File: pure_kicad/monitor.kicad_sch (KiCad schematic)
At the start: 48 parts, among them J3 XT60M, J4 XT60M, J5 Conn_01x04_Pin, J6 Conn_01x04_Pin, J7 Pack Thermistor 1, J8 Pack Thermistor 2, Q5 Q_PMOS_SGD, Q6 Q_NMOS_DGS, Q7 Q_NMOS_DGS, U2 BQ40Z80RSMR

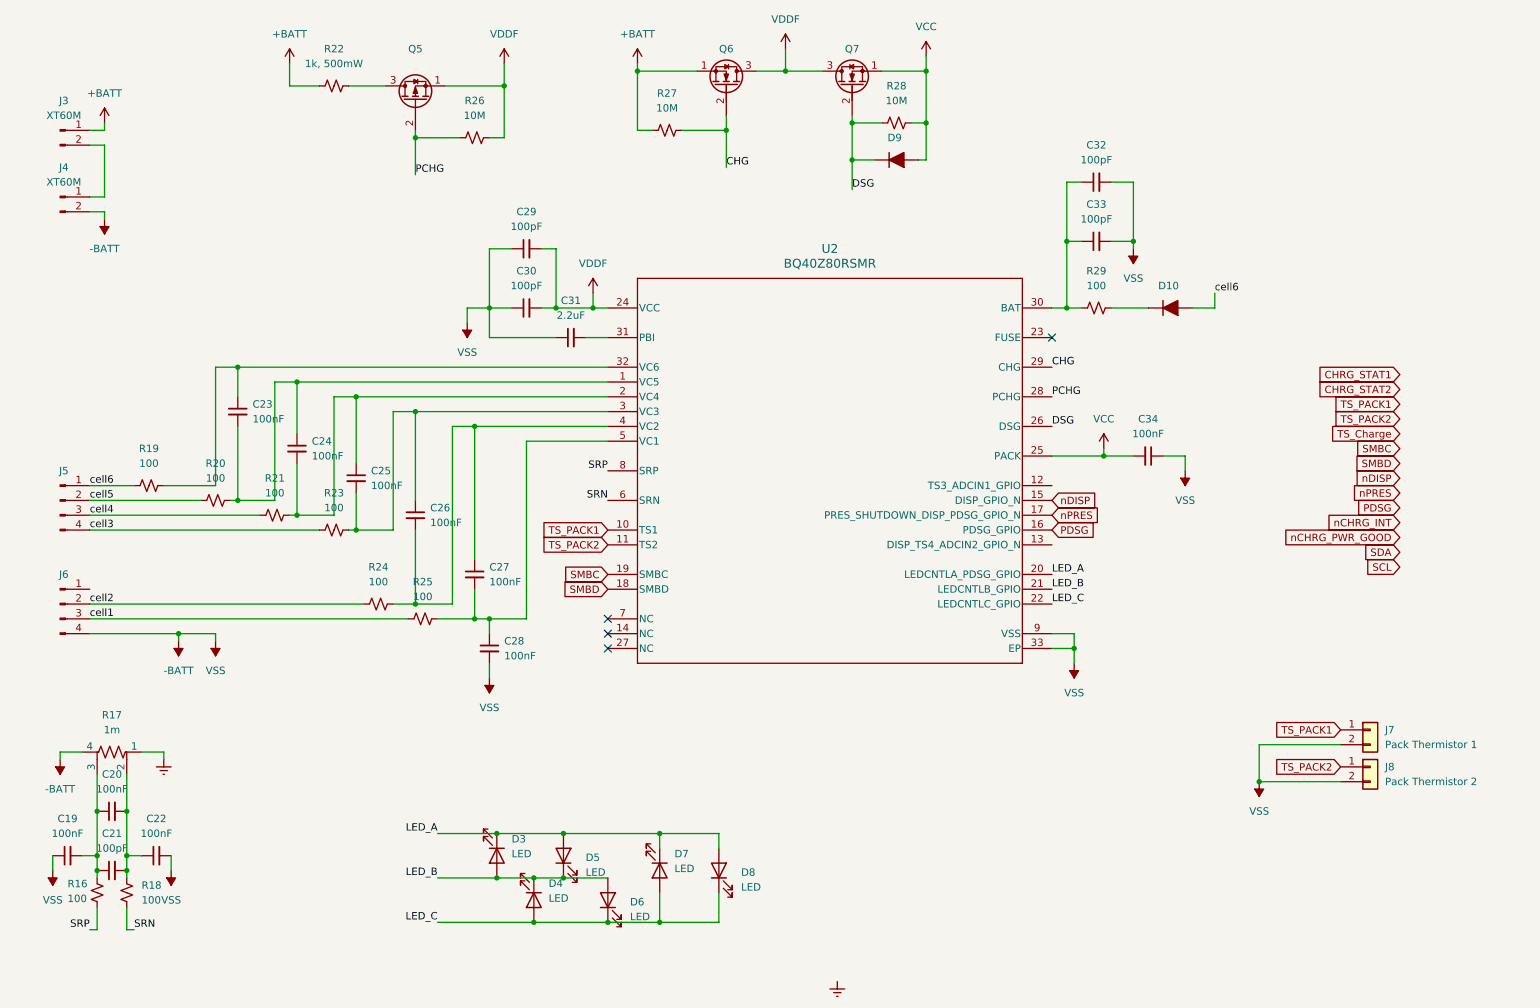
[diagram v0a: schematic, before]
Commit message: Switch to single xt30 and JST B7B for pack, and add thermistor headers
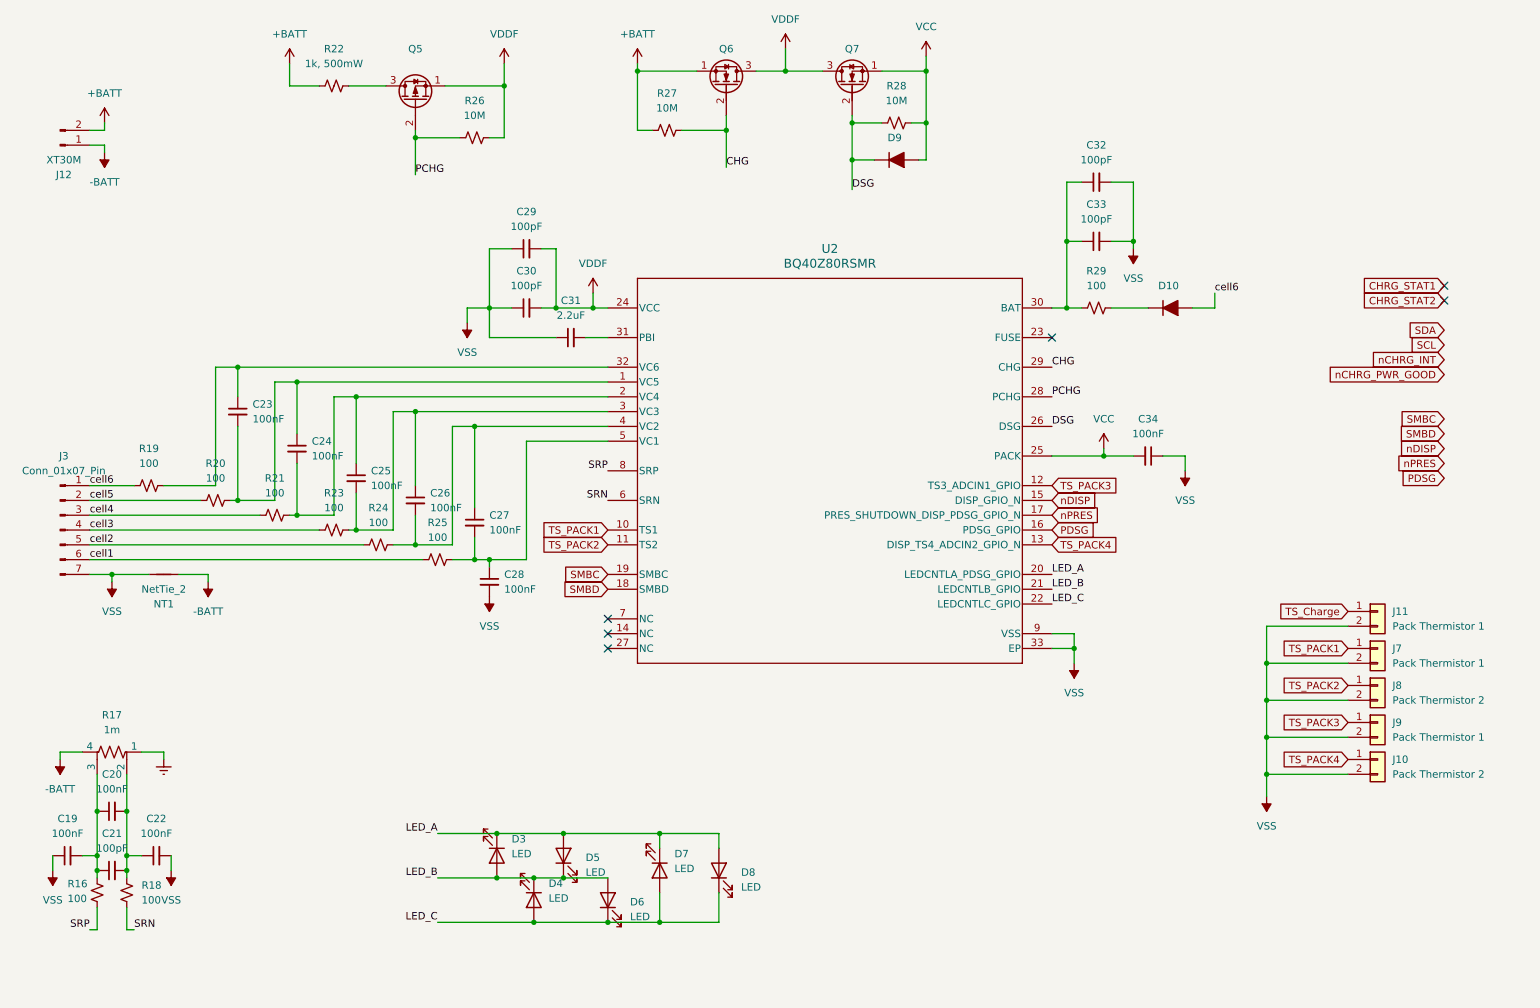
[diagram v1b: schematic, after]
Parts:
- removed J3, J4: XT60M, cyberec:AMASS_XT60-M_1x02_P7.20mm_Vertical, symbol Connector:Conn_01x02_Pin
- removed J5, J6: Conn_01x04_Pin, cyberec:JST_XH_B4B-XH-A_1x04_P2.50mm_Vertical, symbol Connector:Conn_01x04_Pin
- added J10: Pack Thermistor 2, Connector_PinHeader_2.00mm:PinHeader_1x02_P2.00mm_Vertical, symbol Connector_Generic:Conn_01x02
- added J11, J9: Pack Thermistor 1, Connector_PinHeader_2.00mm:PinHeader_1x02_P2.00mm_Vertical, symbol Connector_Generic:Conn_01x02
- added J12: XT30M, cyberec:AMASS_XT30U-M_1x02_P5.0mm_Vertical, symbol Connector:Conn_01x02_Pin
- added J3: Conn_01x07_Pin, cyberec:JST_XH_B7B-XH-AM_1x07_P2.50mm_Vertical, symbol Connector:Conn_01x07_Pin
- added NT1: NetTie_2, NetTie:NetTie-2_SMD_Pad2.0mm, symbol Device:NetTie_2
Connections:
- net +BATT: now also J12.2 (Pin_2)
- net -BATT: now also J12.1 (Pin_1), NT1.2; no longer C19.1, C22.2, C28.2, C29.1, C30.1, C31.1, C32.2, C33.2, C34.1, J7.2 (Pin_2), J8.2 (Pin_2), U2.33 (EP), U2.9 (VSS)
- net TS_Charge: now also J11.1 (Pin_1)
- net cell1: now also J3.6 (Pin_6)
- net cell2: now also J3.5 (Pin_5)
- net cell3: now also J3.4 (Pin_4)
- net cell4: now also J3.3 (Pin_3)
- net cell5: now also J3.2 (Pin_2)
- net cell6: now also J3.1 (Pin_1)
- net TS_PACK3: now reaches U2.12 (TS3_ADCIN1_GPIO)
- net TS_PACK3: now also J9.1 (Pin_1)
- net TS_PACK4: now reaches U2.13 (DISP_TS4_ADCIN2_GPIO_N)
- net TS_PACK4: now also J10.1 (Pin_1)
- new net VSS: C19.1, C22.2, C28.2, C29.1, C30.1, C31.1, C32.2, C33.2, C34.1, J10.2 (Pin_2), J11.2 (Pin_2), J3.7 (Pin_7), J7.2 (Pin_2), J8.2 (Pin_2), J9.2 (Pin_2), NT1.1, U2.33 (EP), U2.9 (VSS)
- no-connect marks 4 -> 6
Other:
- moved on the sheet: C26, C27, C28, J7, J8, R24, R25

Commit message: Added so many pins
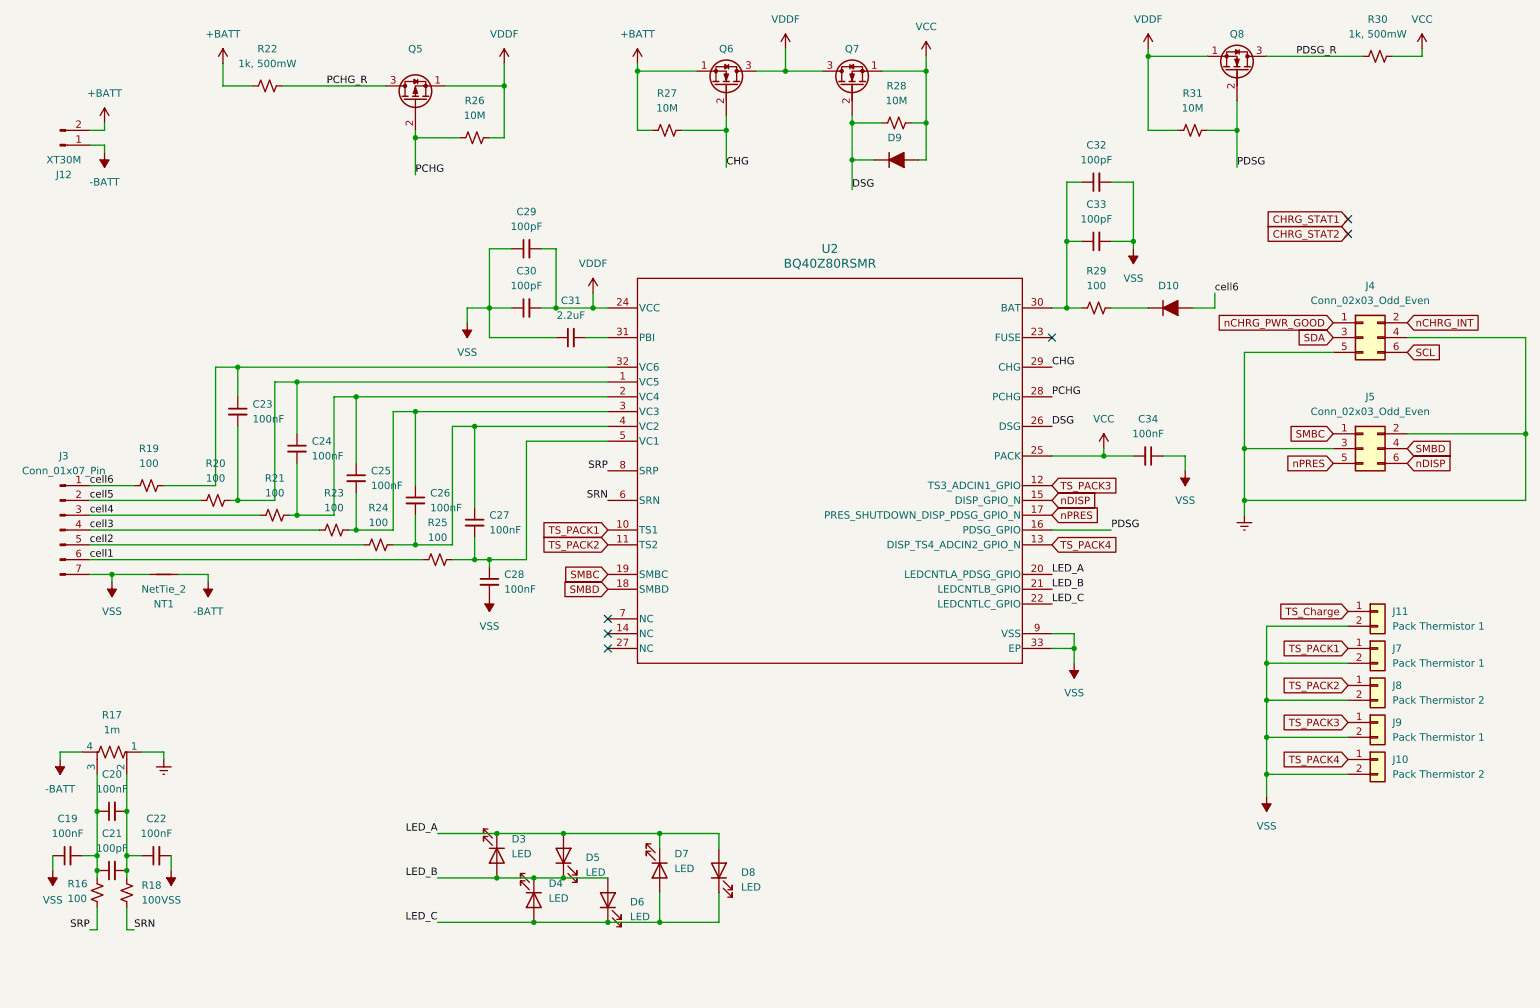
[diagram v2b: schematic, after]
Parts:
- added J4, J5: Conn_02x03_Odd_Even, Connector_PinHeader_2.54mm:PinHeader_2x03_P2.54mm_Vertical, symbol Connector_Generic:Conn_02x03_Odd_Even
- added Q8: Q_NMOS_DGS, cyberec:DFN-8_L3.0-W3.0-P0.65-BL-4, symbol Transistor_FET:Q_NMOS_SGD
- added R30: 1k, 500mW, cyberec:R_1210_3225Metric_Pad1.30x2.65mm_HandSolder, symbol Device:R_Small_US
- added R31: 10M, cyberec:R_0402_1005Metric_Pad0.72x0.64mm_HandSolder, symbol Device:R_Small_US
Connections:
- net Earth: now also J4.4 (Pin_4), J4.5 (Pin_5), J5.2 (Pin_2), J5.3 (Pin_3)
- net PDSG: now also Q8.2 (G), R31.1
- net SCL: now also J4.6 (Pin_6)
- net SDA: now also J4.3 (Pin_3)
- net SMBC: now also J5.1 (Pin_1)
- net SMBD: now also J5.4 (Pin_4)
- net VCC: now also R30.1
- net VDDF: now also Q8.1 (S), R31.2
- net nCHRG_INT: now also J4.2 (Pin_2)
- net nCHRG_PWR_GOOD: now also J4.1 (Pin_1)
- net nDISP: now also J5.6 (Pin_6)
- net nPRES: now also J5.5 (Pin_5)
- net PCHG_R: now reaches Q5.3 (D), R22.1
- new net PDSG_R: Q8.3 (D), R30.2
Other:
- moved on the sheet: R22

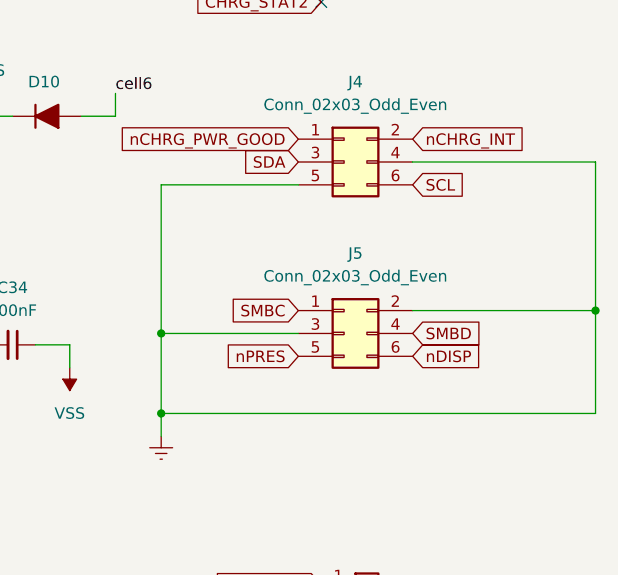
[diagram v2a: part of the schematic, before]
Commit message: Move IO to bottom edge, clean up routing, labels
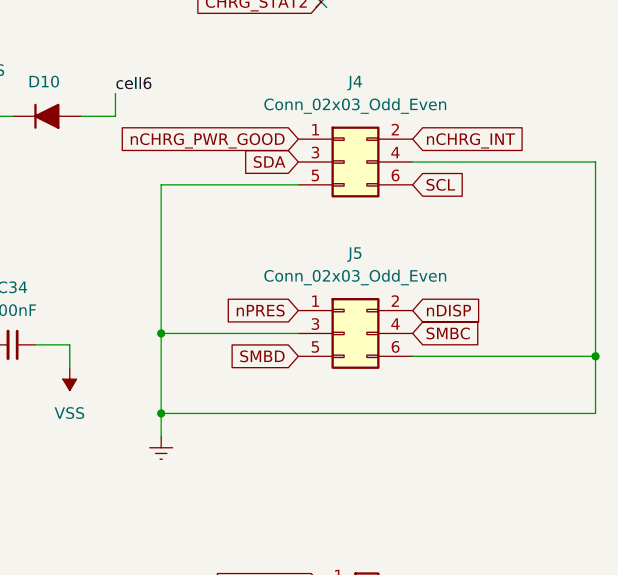
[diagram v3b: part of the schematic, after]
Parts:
- J4, J5: footprint Connector_PinHeader_2.54mm:PinHeader_2x03_P2.54mm_Vertical -> Connector_PinHeader_1.27mm:PinHeader_2x03_P1.27mm_Vertical
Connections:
- net Earth: now also J5.6 (Pin_6); no longer J5.2 (Pin_2)
- net SMBC: now also J5.4 (Pin_4); no longer J5.1 (Pin_1)
- net SMBD: now also J5.5 (Pin_5); no longer J5.4 (Pin_4)
- net nDISP: now also J5.2 (Pin_2); no longer J5.6 (Pin_6)
- net nPRES: now also J5.1 (Pin_1); no longer J5.5 (Pin_5)
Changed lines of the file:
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@@
 	)
 	(junction
+		(at 281.94 100.33)
+		(diameter 0)
+		(color 0 0 0 0)
+	)
+	(junction
 		(at 116.84 163.83)
 		(diameter 0)
@@
 	)
 	(junction
-		(at 281.94 95.25)
-		(diameter 0)
-		(color 0 0 0 0)
-	)
-	(junction
 		(at 39.37 119.38)
 		(diameter 0)
@@
 	(wire
 		(pts
-			(xy 281.94 95.25) (xy 281.94 106.68)
+			(xy 281.94 78.74) (xy 281.94 100.33)
 		)
 		(stroke
@@
 	(wire
 		(pts
-			(xy 281.94 78.74) (xy 281.94 95.25)
-		)
-		(stroke
-			(width 0)
-			(type default)
-		)
-	)
-	(wire
-		(pts
 			(xy 237.49 153.67) (xy 251.46 153.67)
 		)
@@
 	(wire
 		(pts
+			(xy 281.94 100.33) (xy 281.94 106.68)
+		)
+		(stroke
+			(width 0)
+			(type default)
+		)
+	)
+	(wire
+		(pts
 			(xy 222.25 43.18) (xy 217.17 43.18)
 		)
@@
 	(wire
 		(pts
-			(xy 281.94 95.25) (xy 261.62 95.25)
+			(xy 281.94 100.33) (xy 261.62 100.33)
 		)
 		(stroke
@@
 	(global_label "nDISP"
 		(shape input)
-		(at 261.62 100.33 0)
+		(at 261.62 95.25 0)
 		(fields_autoplaced yes)
 		(effects
@@
 		)
 		(property "Intersheetrefs" "${INTERSHEET_REFS}"
-			(at 270.1085 100.33 0)
+			(at 270.1085 95.25 0)
 			(effects
 				(font
@@
 	(global_label "SMBD"
 		(shape input)
-		(at 261.62 97.79 0)
+		(at 248.92 100.33 180)
 		(fields_autoplaced yes)
 		(effects
@@
 				(size 1.27 1.27)
 			)
-			(justify left)
+			(justify right)
 		)
 		(property "Intersheetrefs" "${INTERSHEET_REFS}"
-			(at 269.8061 97.79 0)
+			(at 240.7339 100.33 0)
 			(effects
 				(font
 					(size 1.27 1.27)
 				)
-				(justify left)
+				(justify right)
 				(hide yes)
 			)
@@
 	(global_label "SMBC"
 		(shape input)
-		(at 248.92 95.25 180)
+		(at 261.62 97.79 0)
 		(fields_autoplaced yes)
 		(effects
@@
 				(size 1.27 1.27)
 			)
-			(justify right)
+			(justify left)
 		)
 		(property "Intersheetrefs" "${INTERSHEET_REFS}"
-			(at 240.7339 95.25 0)
+			(at 269.8061 97.79 0)
 			(effects
 				(font
 					(size 1.27 1.27)
 				)
-				(justify right)
+				(justify left)
 				(hide yes)
 			)
@@
 	(global_label "nPRES"
 		(shape input)
-		(at 248.92 100.33 180)
+		(at 248.92 95.25 180)
 		(fields_autoplaced yes)
 		(effects
@@
 		)
 		(property "Intersheetrefs" "${INTERSHEET_REFS}"
-			(at 239.8873 100.33 0)
+			(at 239.8873 95.25 0)
 			(effects
 				(font
@@
 			)
 		)
-		(property "Footprint" "Connector_PinHeader_2.54mm:PinHeader_2x03_P2.54mm_Vertical"
+		(property "Footprint" "Connector_PinHeader_1.27mm:PinHeader_2x03_P1.27mm_Vertical"
 			(at 254 97.79 0)
 			(effects
@@
 			)
 		)
-		(property "Footprint" "Connector_PinHeader_2.54mm:PinHeader_2x03_P2.54mm_Vertical"
+		(property "Footprint" "Connector_PinHeader_1.27mm:PinHeader_2x03_P1.27mm_Vertical"
 			(at 254 78.74 0)
 			(effects
